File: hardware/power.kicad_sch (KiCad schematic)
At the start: 19 parts, among them J3 USB_C_Receptacle_USB2.0_16P, U10 LM317, U11 CH224K, U12 LM317

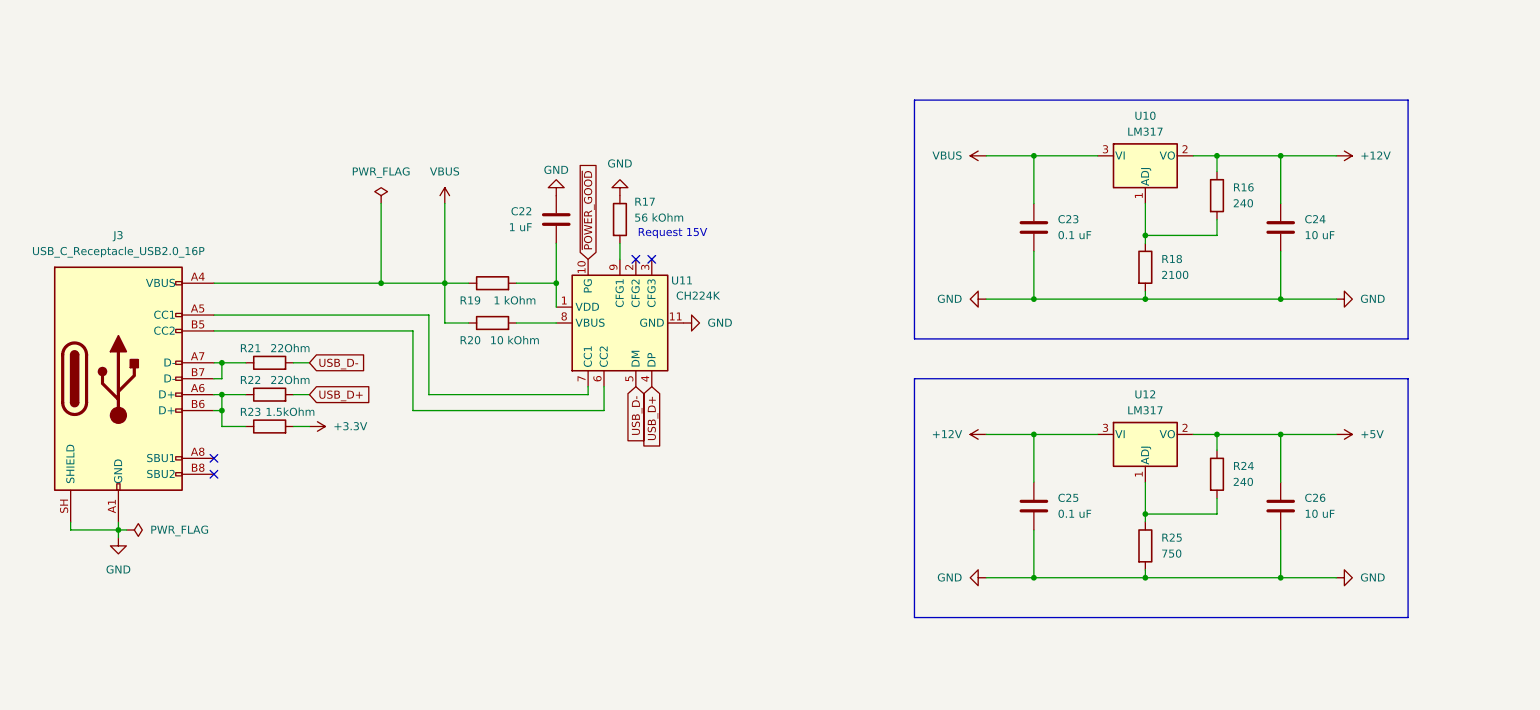
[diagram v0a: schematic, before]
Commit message: hardware: add more capacitors, fix critical mistakes in schematic
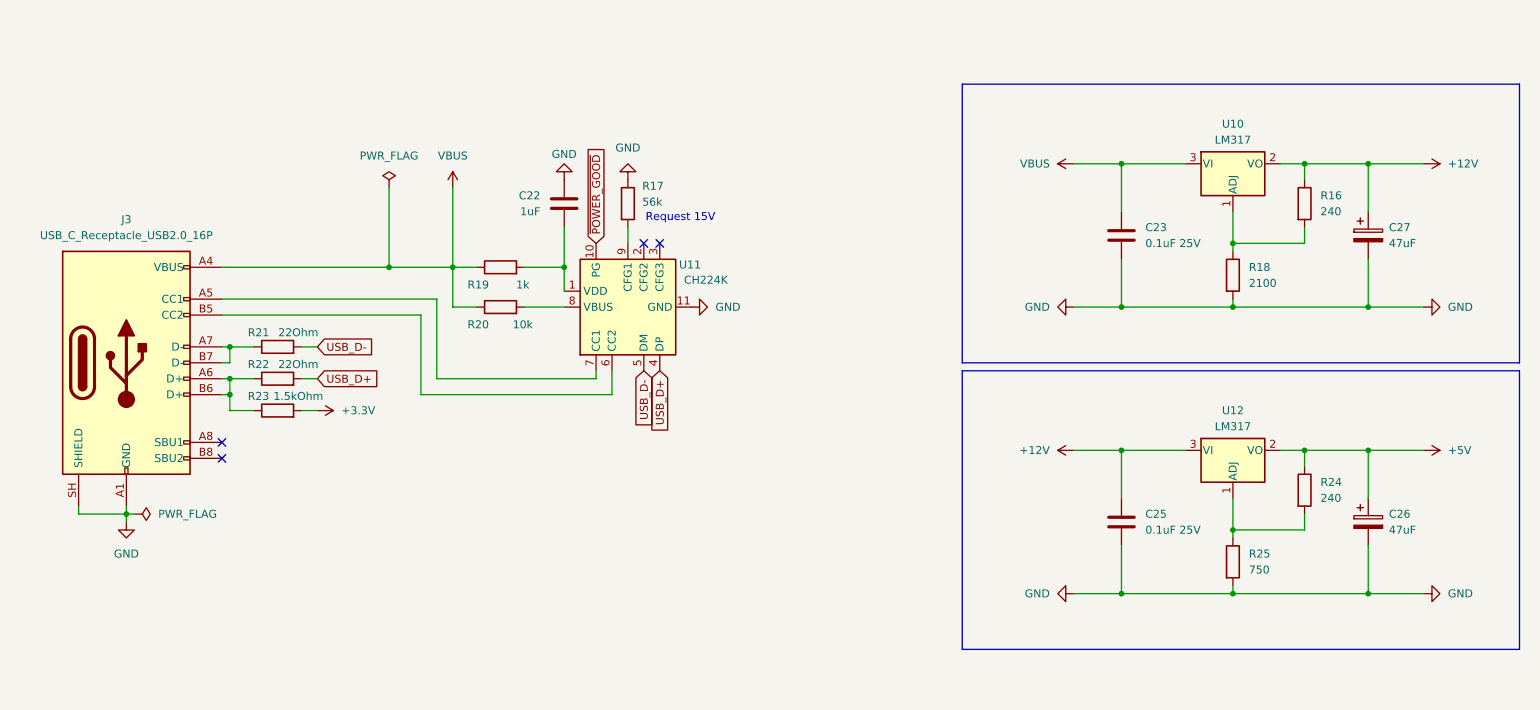
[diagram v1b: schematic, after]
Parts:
- removed C24, C26: 10 uF, symbol Device:C
- added C26, C27: 47uF, Capacitor_THT:CP_Radial_D5.0mm_P2.00mm, symbol Device:C_Polarized
- C22: value 1 uF -> 1uF
- C23, C25: value 0.1 uF -> 0.1uF 25V; footprint (none) -> Capacitor_THT:C_Disc_D7.0mm_W2.5mm_P5.00mm
- J3: footprint (none) -> Connector_USB:USB_C_Receptacle_HRO_TYPE-C-31-M-12
- R17: value 56 kOhm -> 56k
- R19: value 1 kOhm -> 1k
- R20: value 10 kOhm -> 10k
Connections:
- net +12V: now also C27.1
- net +5V: now also C26.1
- net GND: now also C26.2, C27.2
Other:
- moved on the sheet: C22, C23, J3, R16, R17, R18, R19, R20, R21, R22, R23, R24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

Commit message: hardware: connect MBM module like Compass
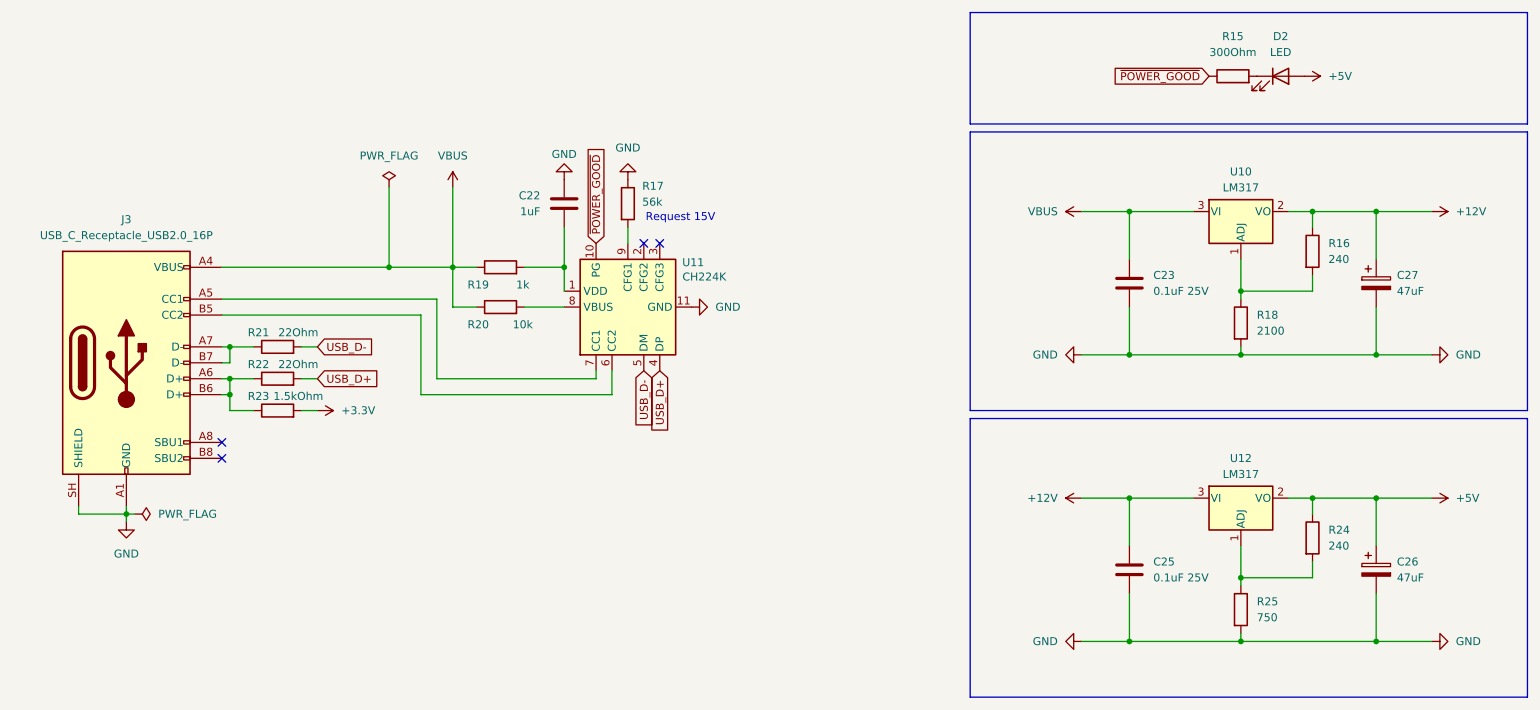
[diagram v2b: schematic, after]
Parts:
- added D2: LED, LED_SMD:LED_0805_2012Metric_Pad1.15x1.40mm_HandSolder, symbol Device:LED
- added R15: 300Ohm, Resistor_SMD:R_0805_2012Metric_Pad1.20x1.40mm_HandSolder, symbol Device:R
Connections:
- net +5V: now also D2.2 (A)
- net ~{POWER_GOOD}: now also R15.1
- new net: D2.1 (K), R15.2
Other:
- moved on the sheet: C23, C25, C26, C27, R16, R18, R24, R25, U10, U12

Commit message: hardware: add powerfail circuit, rework power
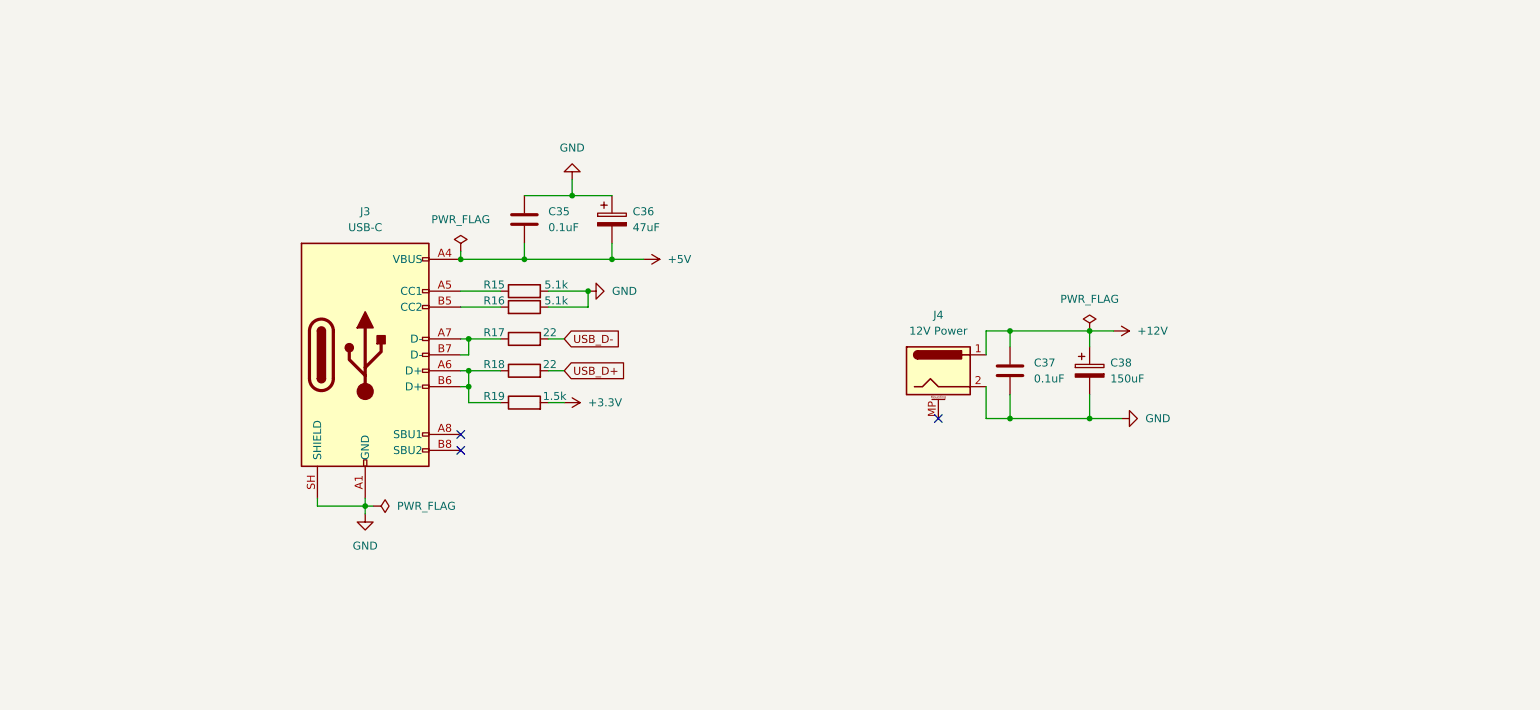
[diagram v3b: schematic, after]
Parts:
- removed C22: 1uF, Capacitor_SMD:C_0805_2012Metric_Pad1.18x1.45mm_HandSolder, symbol Device:C
- removed C23, C25: 0.1uF 25V, Capacitor_THT:C_Disc_D7.0mm_W2.5mm_P5.00mm, symbol Device:C
- removed C26, C27: 47uF, Capacitor_THT:CP_Radial_D5.0mm_P2.00mm, symbol Device:C_Polarized
- removed D2: LED, LED_SMD:LED_0805_2012Metric_Pad1.15x1.40mm_HandSolder, symbol Device:LED
- removed R17: 56k, Resistor_SMD:R_0805_2012Metric_Pad1.20x1.40mm_HandSolder, symbol Device:R
- removed R18: 2100, Resistor_SMD:R_0805_2012Metric_Pad1.20x1.40mm_HandSolder, symbol Device:R
- removed R19: 1k, Resistor_SMD:R_0805_2012Metric_Pad1.20x1.40mm_HandSolder, symbol Device:R
- removed R20: 10k, Resistor_SMD:R_0805_2012Metric_Pad1.20x1.40mm_HandSolder, symbol Device:R
- removed R24: 240, Resistor_SMD:R_0805_2012Metric_Pad1.20x1.40mm_HandSolder, symbol Device:R
- removed R25: 750, Resistor_SMD:R_0805_2012Metric_Pad1.20x1.40mm_HandSolder, symbol Device:R
- removed U10, U12: LM317, Package_TO_SOT_THT:TO-220-3_Vertical, symbol Regulator_Linear:LM317_TO-220
- removed U11: CH224K, Package_SO:SSOP-10-1EP_3.9x4.9mm_P1mm_EP2.1x3.3mm, symbol Interface_USB:CH224K
- added C35, C37: 0.1uF, Capacitor_SMD:C_0805_2012Metric_Pad1.18x1.45mm_HandSolder, symbol Device:C
- added C36: 47uF, Capacitor_THT:CP_Radial_D5.0mm_P2.00mm, symbol Device:C_Polarized
- added C38: 150uF, Capacitor_THT:CP_Radial_D10.0mm_P2.50mm, symbol Device:C_Polarized
- added J4: 12V Power, Connector_BarrelJack:BarrelJack_Horizontal, symbol Connector:Barrel_Jack_MountingPin
- J3: value USB_C_Receptacle_USB2.0_16P -> USB-C
- R15: value 300Ohm -> 5.1k
- R16: value 240 -> 5.1k
- R17: renamed from R21; value 22Ohm -> 22
- R18: renamed from R22; value 22Ohm -> 22
- R19: renamed from R23; value 1.5kOhm -> 1.5k
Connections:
- net VBUS is gone; now on net +5V: J3.A4 (VBUS), J3.A9 (VBUS), J3.B4 (VBUS), J3.B9 (VBUS)
- net ~{POWER_GOOD} is gone; now on an unnamed net: R15.1
- net +12V: now also C37.1, C38.1, J4.1; no longer R16.1
- net +5V: now also C35.2, C36.2
- net GND: now also R15.2, R16.1, C35.1, C36.1, C37.2, C38.2, J4.2
- net at R16.2: now also J3.B5 (CC2)
- no-connect marks 4 -> 3
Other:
- note removed: "Request 15V"
- moved on the sheet: J3, R17, R18, R19

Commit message: hardware: connect input signals from 7220 to stm32 five tolerant pins
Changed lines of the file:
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@@
 	)
 	(global_label "USB_D+"
-		(shape input)
+		(shape bidirectional)
 		(at 121.92 100.33 0)
 		(fields_autoplaced yes)
@@
 		)
 		(property "Intersheetrefs" "${INTERSHEET_REFS}"
-			(at 132.5252 100.33 0)
+			(at 133.6365 100.33 0)
 			(hide yes)
 			(show_name no)
@@
 	)
 	(global_label "USB_D-"
-		(shape input)
+		(shape bidirectional)
 		(at 121.92 95.25 0)
 		(fields_autoplaced yes)
@@
 		)
 		(property "Intersheetrefs" "${INTERSHEET_REFS}"
-			(at 132.5252 95.25 0)
+			(at 133.6365 95.25 0)
 			(hide yes)
 			(show_name no)
